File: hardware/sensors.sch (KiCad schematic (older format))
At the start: 17 parts

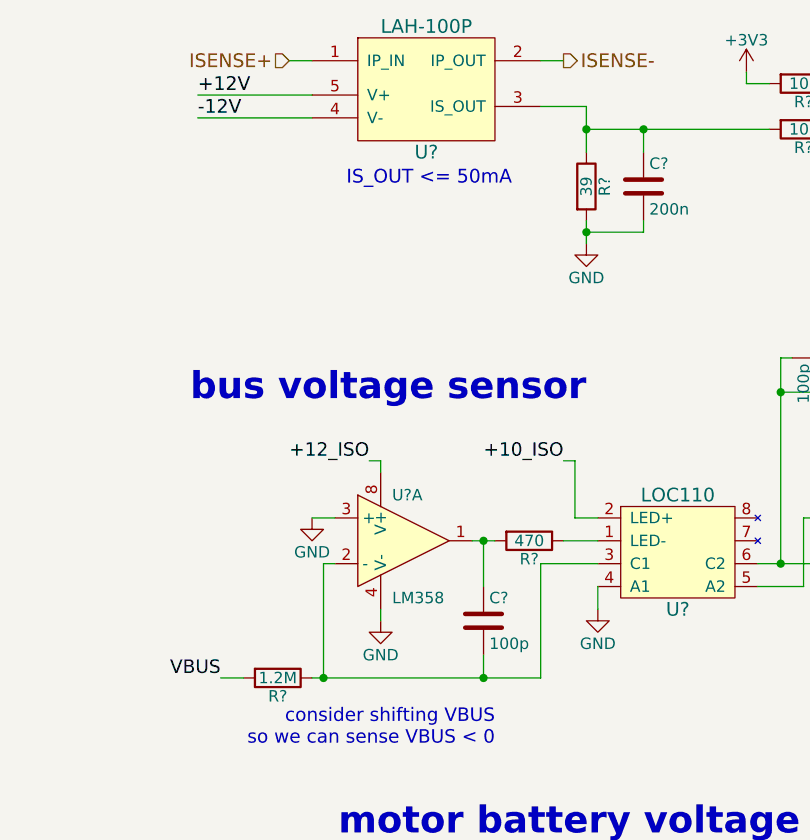
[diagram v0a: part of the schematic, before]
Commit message: HW: change tm4c1294ncpdt to kcpdt; change LT3487 to 3471
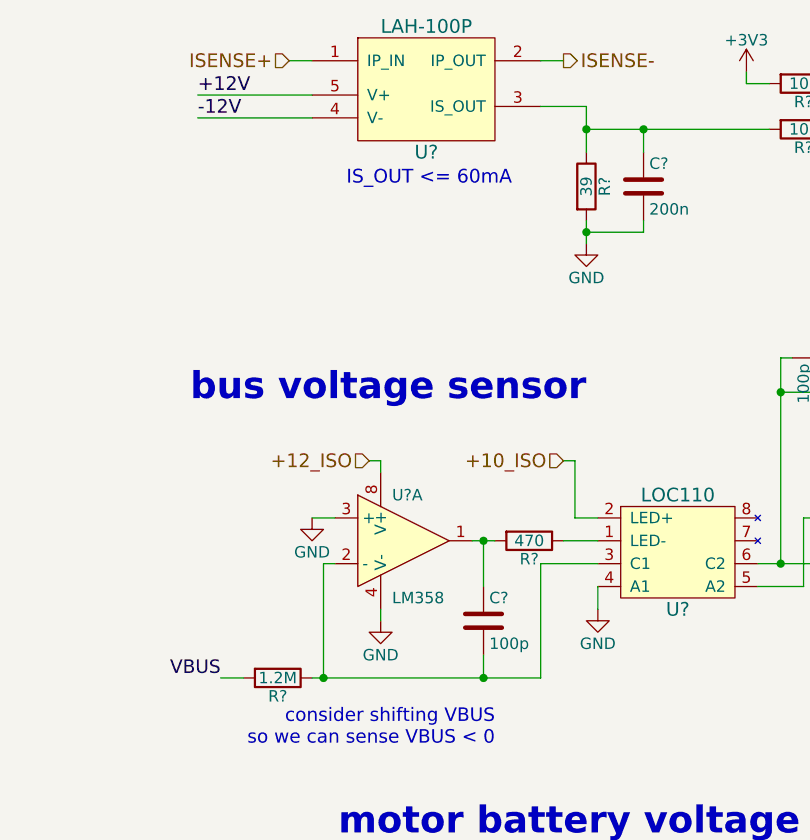
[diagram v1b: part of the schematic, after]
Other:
- note added: "IS_OUT <= 60mA"
- note removed: "IS_OUT <= 50mA"
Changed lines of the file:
@@
 $EndComp
 Text Notes 1350 1600 0    60   ~ 0
-IS_OUT <= 50mA
+IS_OUT <= 60mA
 Text HLabel 1100 1050 0    60   Input ~ 0
 ISENSE+
@@
 	1    0    0    -1
 $EndComp
-Text Label 1450 2800 2    59   ~ 0
-+12_ISO
 $Comp
 L GND #PWR?
@@
 	2450 3250 2200 3250
 Wire Wire Line
-	2200 3750 2200 3250
-Wire Wire Line
-	1200 3750 2200 3750
+	2200 3250 2200 3750
+Wire Wire Line
+	2200 3750 1200 3750
 Wire Wire Line
 	1250 3750 1250 3250
@@
 Wire Wire Line
 	1500 2800 1450 2800
-Text Label 2300 2800 2    59   ~ 0
-+10_ISO
 Wire Wire Line
 	2350 2800 2300 2800
@@
 Text Notes 9700 5250 2    59   ~ 0
 signswise: NPN open collector\nsome others: differential
+Text HLabel 1450 2800 0    60   Input ~ 0
++12_ISO
+Text HLabel 2300 2800 0    60   Input ~ 0
++10_ISO
 $EndSCHEMATC

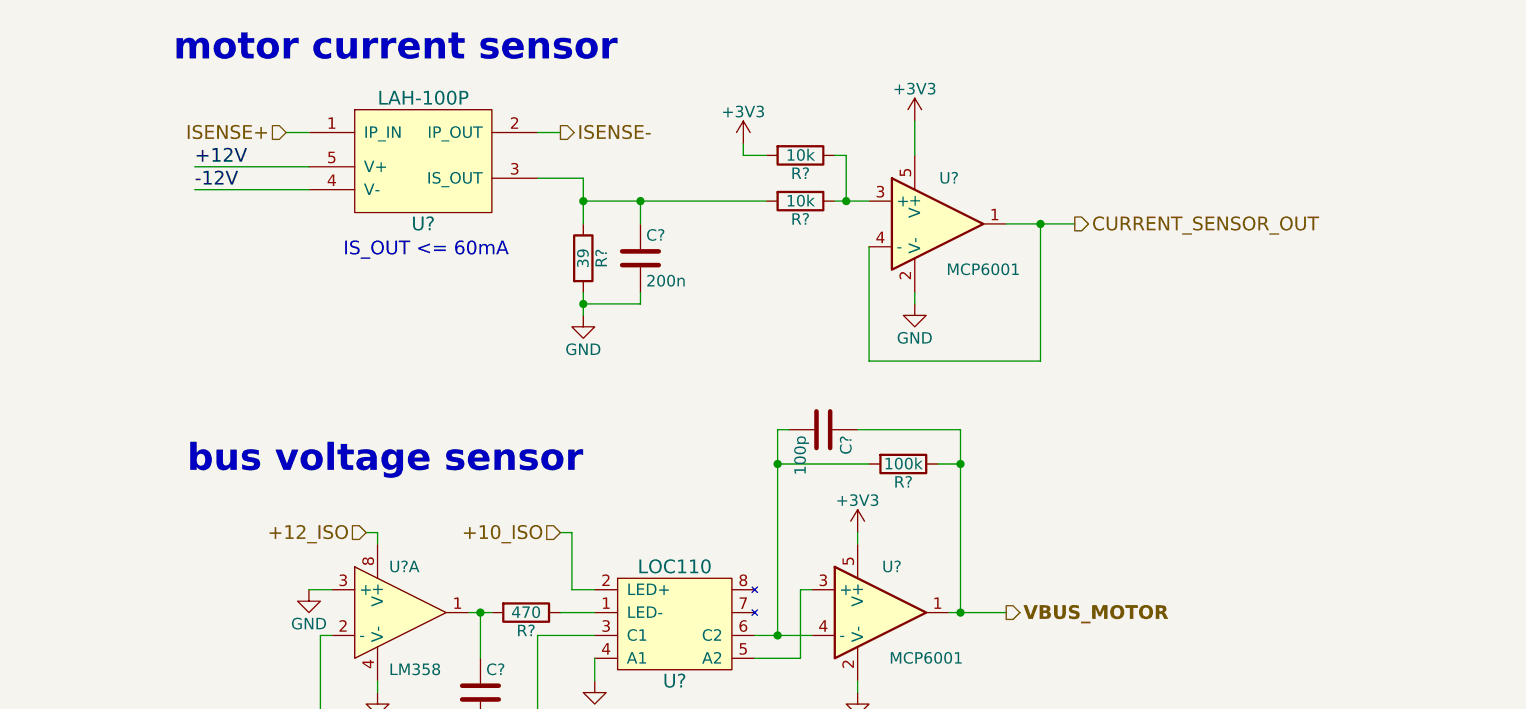
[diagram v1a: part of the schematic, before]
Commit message: cleaned up h-bridge; added digital isolators
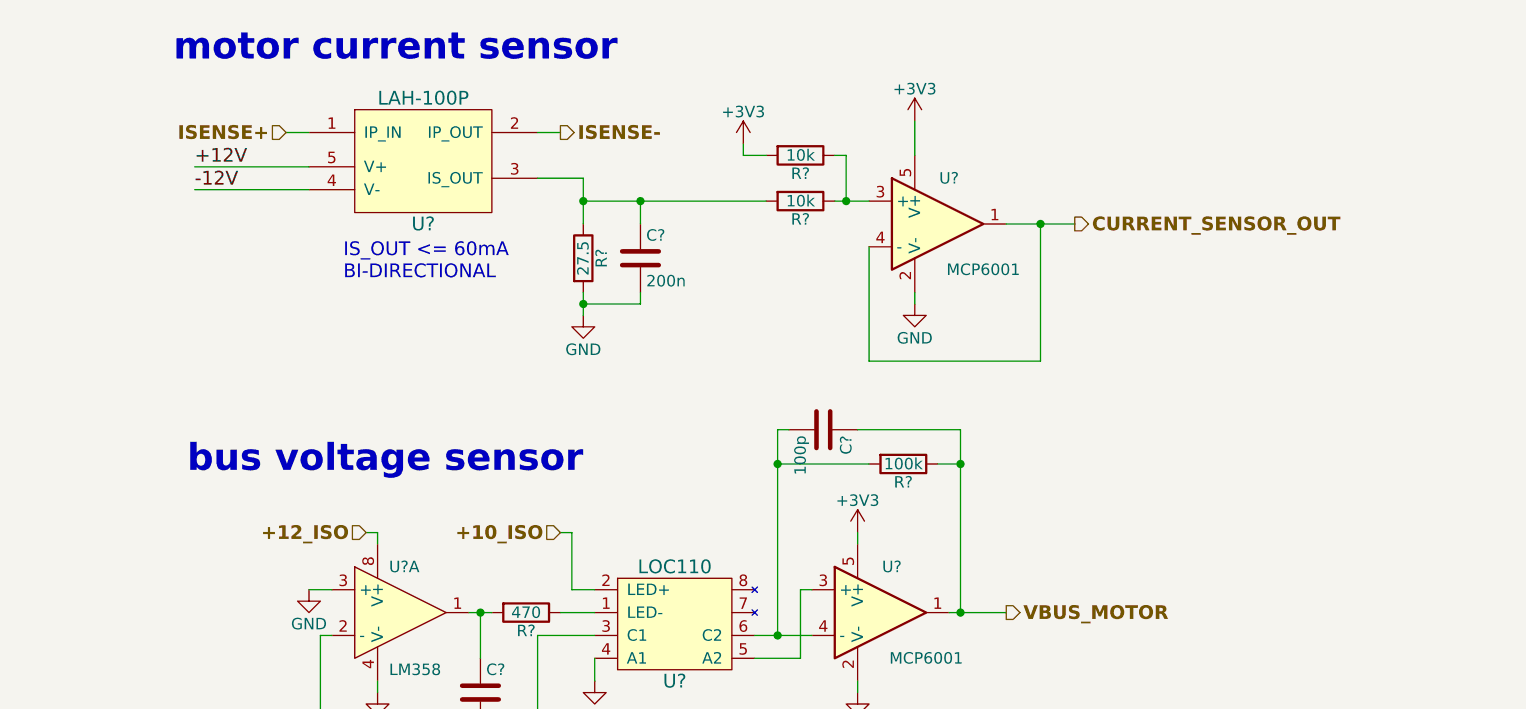
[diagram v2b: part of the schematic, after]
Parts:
- R?: value 39 -> 27.5
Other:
- note added: "IS_OUT <= 60mA\nBI-DIRECTIONAL"
- note removed: "IS_OUT <= 60mA"
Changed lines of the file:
@@
 P 2400 1600
 F 0 "R?" V 2480 1600 50  0000 C CNN
-F 1 "39" V 2400 1600 50  0000 C CNN
+F 1 "27.5" V 2400 1600 50  0000 C CNN
 F 2 "" V 2330 1600 50  0000 C CNN
 F 3 "" H 2400 1600 50  0000 C CNN
@@
 $EndComp
 $Comp
-L GND #PWR?
+L GND #PWR010
 U 1 1 5975C471
 P 2400 1850
-F 0 "#PWR?" H 2400 1600 50  0001 C CNN
+F 0 "#PWR010" H 2400 1600 50  0001 C CNN
 F 1 "GND" H 2400 1700 50  0000 C CNN
 F 2 "" H 2400 1850 50  0000 C CNN
@@
 $EndComp
 $Comp
-L GND #PWR?
+L GND #PWR011
 U 1 1 5975C76F
 P 3850 1800
-F 0 "#PWR?" H 3850 1550 50  0001 C CNN
+F 0 "#PWR011" H 3850 1550 50  0001 C CNN
 F 1 "GND" H 3850 1650 50  0000 C CNN
 F 2 "" H 3850 1800 50  0000 C CNN
@@
 $EndComp
 $Comp
-L +3V3 #PWR?
+L +3V3 #PWR012
 U 1 1 5975C874
 P 3850 1000
-F 0 "#PWR?" H 3850 850 50  0001 C CNN
+F 0 "#PWR012" H 3850 850 50  0001 C CNN
 F 1 "+3V3" H 3850 1140 50  0000 C CNN
 F 2 "" H 3850 1000 50  0000 C CNN
@@
 $EndComp
 $Comp
-L +3V3 #PWR?
+L +3V3 #PWR013
 U 1 1 5975CA4E
 P 3100 1100
-F 0 "#PWR?" H 3100 950 50  0001 C CNN
+F 0 "#PWR013" H 3100 950 50  0001 C CNN
 F 1 "+3V3" H 3100 1240 50  0000 C CNN
 F 2 "" H 3100 1100 50  0000 C CNN
@@
 	1    0    0    -1
 $EndComp
-Text Notes 1350 1600 0    60   ~ 0
-IS_OUT <= 60mA
-Text HLabel 1100 1050 0    60   Input ~ 0
+Text Notes 1350 1700 0    60   ~ 0
+IS_OUT <= 60mA\nBI-DIRECTIONAL
+Text HLabel 1100 1050 0    60   Input ~ 12
 ISENSE+
-Text HLabel 2300 1050 2    60   Output ~ 0
+Text HLabel 2300 1050 2    60   Output ~ 12
 ISENSE-
-Text HLabel 4550 1450 2    60   Output ~ 0
+Text HLabel 4550 1450 2    60   Output ~ 12
 CURRENT_SENSOR_OUT
 Text Notes 2550 750  2    118  ~ 24
@@
 bus voltage sensor
 $Comp
-L +9V #PWR?
+L +9V #PWR014
 U 1 1 597CF4DC
 P 1000 6600
-F 0 "#PWR?" H 1000 6450 50  0001 C CNN
+F 0 "#PWR014" H 1000 6450 50  0001 C CNN
 F 1 "+9V" H 1000 6740 50  0000 C CNN
 F 2 "" H 1000 6600 50  0000 C CNN
@@
 $EndComp
 $Comp
-L GND #PWR?
+L GND #PWR015
 U 1 1 597CFAF9
 P 1000 7450
-F 0 "#PWR?" H 1000 7200 50  0001 C CNN
+F 0 "#PWR015" H 1000 7200 50  0001 C CNN
 F 1 "GND" H 1000 7300 50  0000 C CNN
 F 2 "" H 1000 7450 50  0000 C CNN
@@
 $EndComp
 $Comp
-L +3V3 #PWR?
+L +3V3 #PWR016
 U 1 1 597D01E3
 P 1550 6600
-F 0 "#PWR?" H 1550 6450 50  0001 C CNN
+F 0 "#PWR016" H 1550 6450 50  0001 C CNN
 F 1 "+3V3" H 1550 6740 50  0000 C CNN
 F 2 "" H 1550 6600 50  0000 C CNN
@@
 $EndComp
 $Comp
-L GND #PWR?
+L GND #PWR017
 U 1 1 597D0261
 P 1550 7300
-F 0 "#PWR?" H 1550 7050 50  0001 C CNN
+F 0 "#PWR017" H 1550 7050 50  0001 C CNN
 F 1 "GND" H 1550 7150 50  0000 C CNN
 F 2 "" H 1550 7300 50  0000 C CNN
@@
 $EndComp
 $Comp
-L GND #PWR?
+L GND #PWR018
 U 1 1 597E8EB7
 P 1500 3500
-F 0 "#PWR?" H 1500 3250 50  0001 C CNN
+F 0 "#PWR018" H 1500 3250 50  0001 C CNN
 F 1 "GND" H 1500 3350 50  0000 C CNN
 F 2 "" H 1500 3500 50  0000 C CNN
@@
 $EndComp
 $Comp
-L GND #PWR?
+L GND #PWR019
 U 1 1 597E9194
 P 1200 3050
-F 0 "#PWR?" H 1200 2800 50  0001 C CNN
+F 0 "#PWR019" H 1200 2800 50  0001 C CNN
 F 1 "GND" H 1200 2900 50  0000 C CNN
 F 2 "" H 1200 3050 50  0000 C CNN
@@
 $EndComp
 $Comp
-L GND #PWR?
+L GND #PWR020
 U 1 1 597E9761
 P 2450 3450
-F 0 "#PWR?" H 2450 3200 50  0001 C CNN
+F 0 "#PWR020" H 2450 3200 50  0001 C CNN
 F 1 "GND" H 2450 3300 50  0000 C CNN
 F 2 "" H 2450 3450 50  0000 C CNN
@@
 	3150 3250 3400 3250
 $Comp
-L GND #PWR?
+L GND #PWR021
 U 1 1 597EB09C
 P 3600 3500
-F 0 "#PWR?" H 3600 3250 50  0001 C CNN
+F 0 "#PWR021" H 3600 3250 50  0001 C CNN
 F 1 "GND" H 3600 3350 50  0000 C CNN
 F 2 "" H 3600 3500 50  0000 C CNN
@@
 	3600 3450 3600 3500
 $Comp
-L +3V3 #PWR?
+L +3V3 #PWR022
 U 1 1 597EB11C
 P 3600 2800
-F 0 "#PWR?" H 3600 2650 50  0001 C CNN
+F 0 "#PWR022" H 3600 2650 50  0001 C CNN
 F 1 "+3V3" H 3600 2940 50  0000 C CNN
 F 2 "" H 3600 2800 50  0000 C CNN
@@
 Text Notes 9700 5250 2    59   ~ 0
 signswise: NPN open collector\nsome others: differential
-Text HLabel 1450 2800 0    60   Input ~ 0
+Text HLabel 1450 2800 0    60   Input ~ 12
 +12_ISO
-Text HLabel 2300 2800 0    60   Input ~ 0
+Text HLabel 2300 2800 0    60   Input ~ 12
 +10_ISO
 $EndSCHEMATC

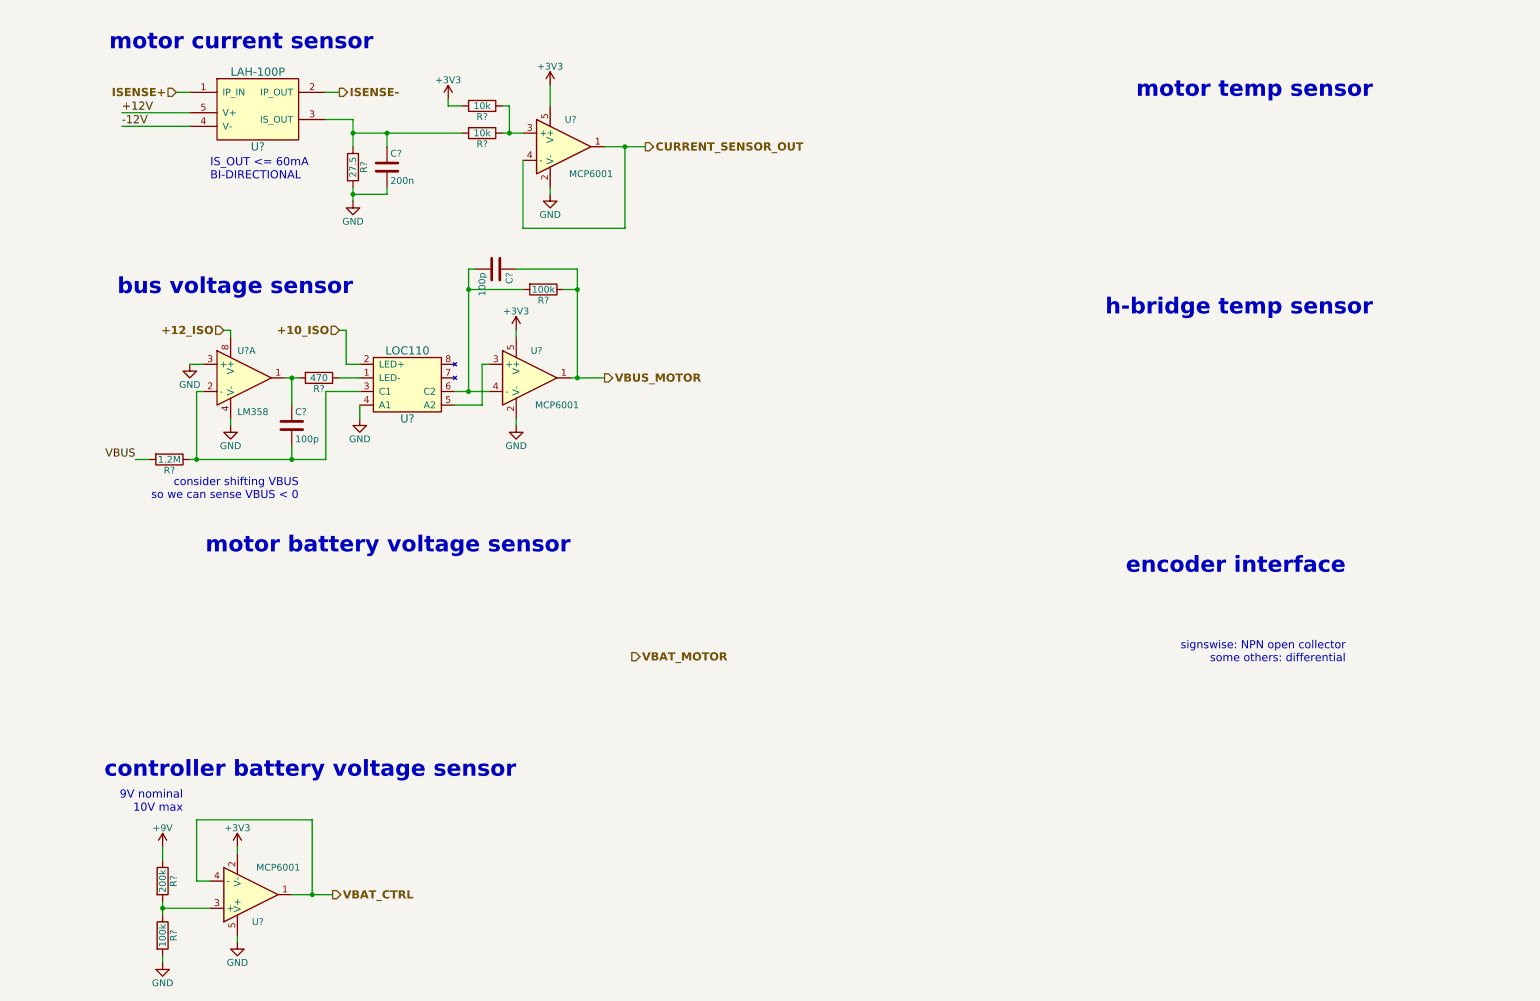
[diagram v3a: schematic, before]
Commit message: ERC cleanup, begin pcbnew population
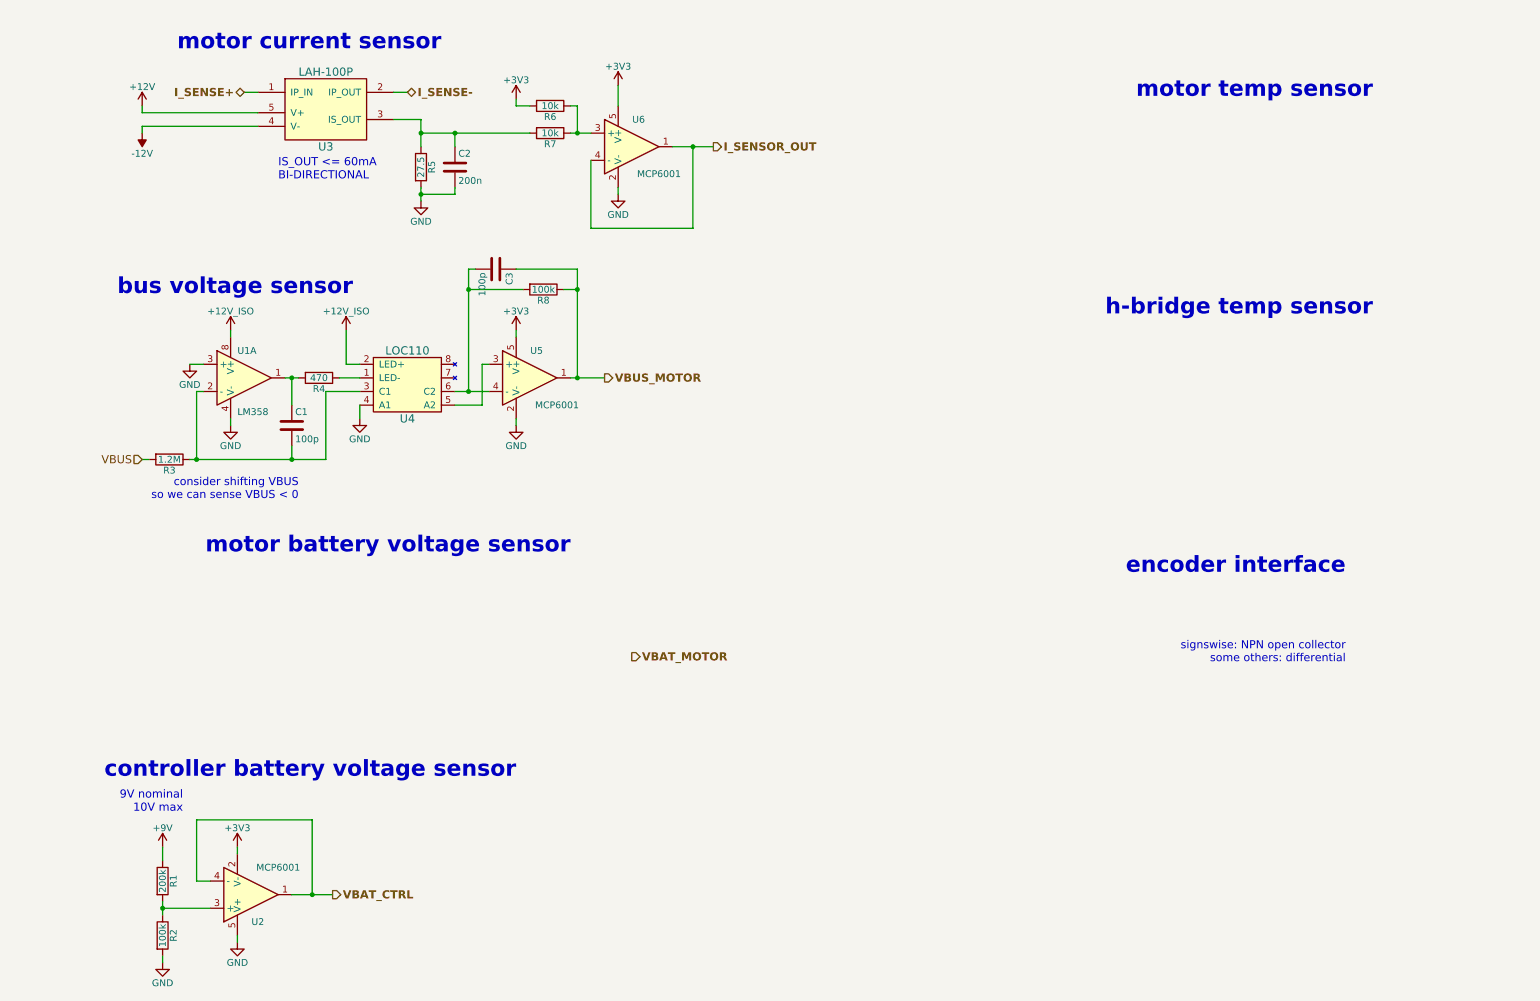
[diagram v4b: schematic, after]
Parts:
- C1, C2, C3: renamed from C?; footprint (none) -> Capacitors_SMD:C_0603
- R1, R2, R3, R4, R5, R6, R7, R8: renamed from R?; footprint (none) -> Resistors_SMD:R_0603
- U1: renamed from U?; footprint (none) -> SMD_Packages:SOIC-8-N
- U2, U5, U6: renamed from U?; footprint (none) -> TO_SOT_Packages_SMD:SC-70-5
- U4: renamed from U?; footprint (none) -> Housings_DIP:DIP-8_W7.62mm
- gave numbers to parts that had none: 1
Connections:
- net +12_ISO is gone; now on net +12V_ISO: U1.8 (V+)
- net +10_ISO renamed +12V_ISO
- net CURRENT_SENSOR_OUT renamed I_SENSOR_OUT
- net ISENSE+ renamed I_SENSE+
- net ISENSE- renamed I_SENSE-
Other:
- moved on the sheet: C2, R5, R6, R7, U3, U6

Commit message: hw: minor tweaks
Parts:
- C1, C3: value 100p -> 47p
- R8: value 100k -> 51k
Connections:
- net GND: now also U4.5 (A2), U5.3 (+)
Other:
- note removed: "consider shifting VBUS\nso we can sense VBUS < 0"
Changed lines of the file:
@@
 P 1950 3500
 F 0 "C1" H 1975 3600 50  0000 L CNN
-F 1 "100p" H 1975 3400 50  0000 L CNN
+F 1 "47p" H 1975 3400 50  0000 L CNN
 F 2 "Capacitors_SMD:C_0603" H 1988 3350 50  0001 C CNN
 F 3 "" H 1950 3500 50  0000 C CNN
@@
 P 3800 2500
 F 0 "R8" V 3880 2500 50  0000 C CNN
-F 1 "100k" V 3800 2500 50  0000 C CNN
+F 1 "51k" V 3800 2500 50  0000 C CNN
 F 2 "Resistors_SMD:R_0603" V 3730 2500 50  0001 C CNN
 F 3 "" H 3800 2500 50  0000 C CNN
@@
 U 1 1 597EB397
 P 3450 2350
-F 0 "C3" H 3475 2450 50  0000 L CNN
-F 1 "100p" H 3475 2250 50  0000 L CNN
+F 0 "C3" V 3400 2450 50  0000 L CNN
+F 1 "47p" V 3400 2150 50  0000 L CNN
 F 2 "Capacitors_SMD:C_0603" H 3488 2200 50  0001 C CNN
 F 3 "" H 3450 2350 50  0000 C CNN
@@
 	0    1    1    0
 $EndComp
-Text Notes 2000 4050 2    59   ~ 0
-consider shifting VBUS\nso we can sense VBUS < 0
 $Comp
 L LM358 U1
@@
 	3400 3050 3350 3050
 Wire Wire Line
-	3350 3050 3350 3350
+	3350 3050 3350 3500
 Wire Wire Line
 	3350 3350 3150 3350
@@
 Wire Wire Line
 	2700 1050 2800 1050
+$Comp
+L GND #PWR?
+U 1 1 599BDED6
+P 3350 3500
+F 0 "#PWR?" H 3350 3250 50  0001 C CNN
+F 1 "GND" H 3350 3350 50  0000 C CNN
+F 2 "" H 3350 3500 50  0000 C CNN
+F 3 "" H 3350 3500 50  0000 C CNN
+	1    3350 3500
+	1    0    0    -1
+$EndComp
+Connection ~ 3350 3350
 $EndSCHEMATC
